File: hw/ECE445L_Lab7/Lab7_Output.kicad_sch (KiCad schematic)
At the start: 4 parts, among them Q1 IRLD024PBF, U2 Adafruit ST7735R

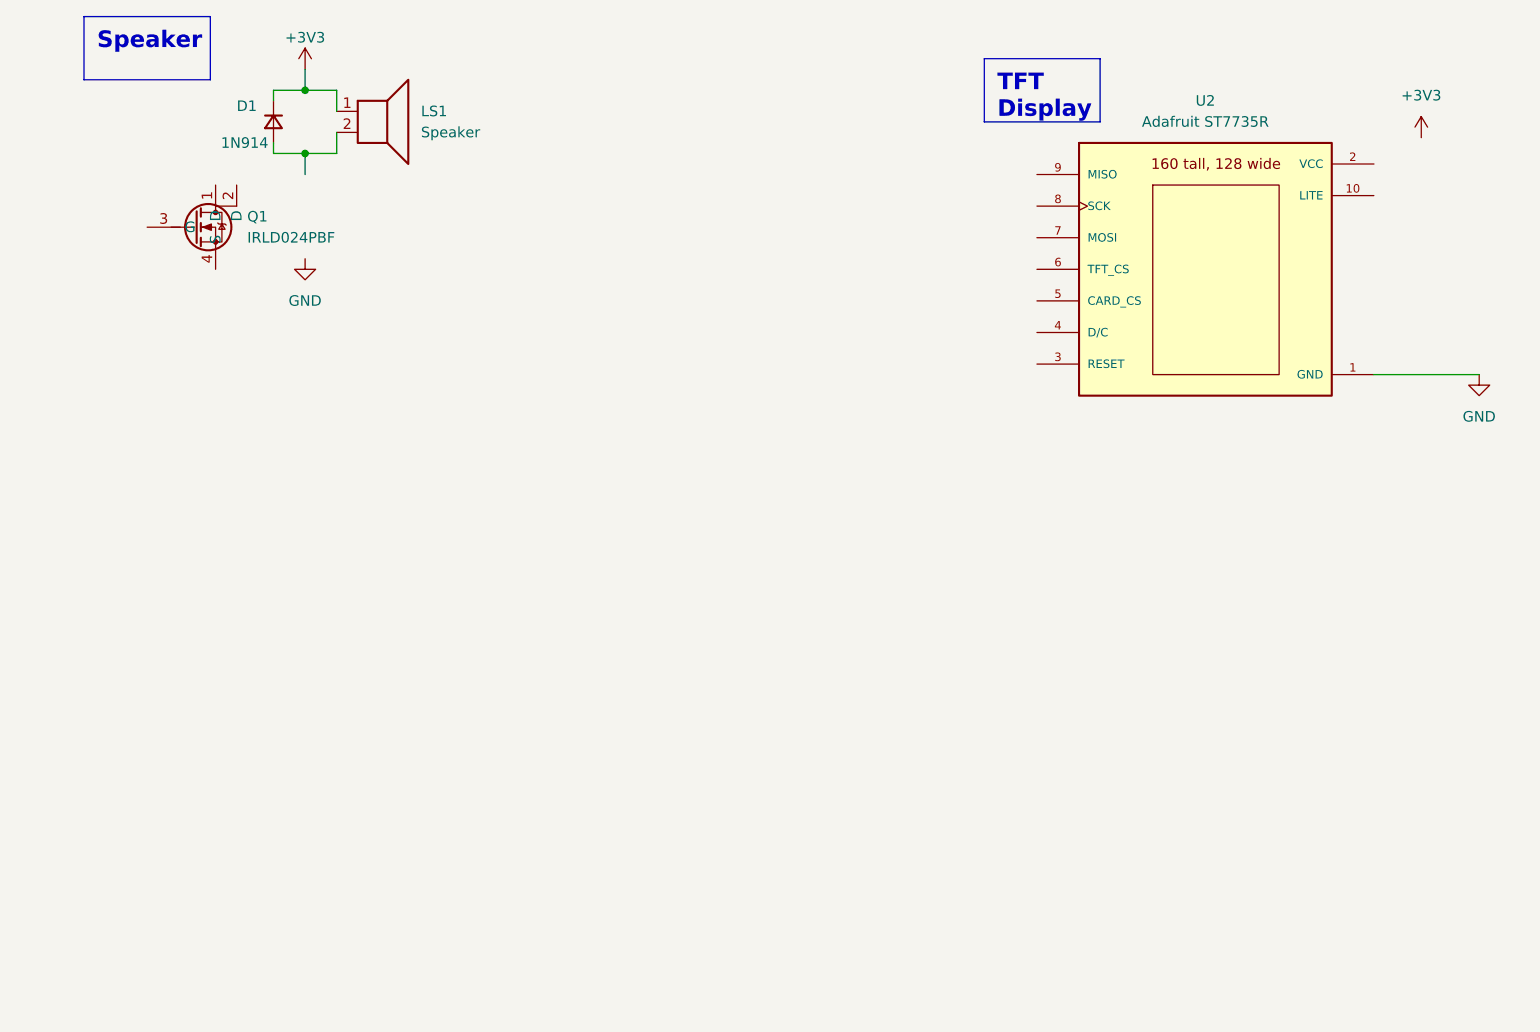
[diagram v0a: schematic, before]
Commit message: Created spice models for analog circuits, started kicad schematic -> right audio channel, screen, basic power
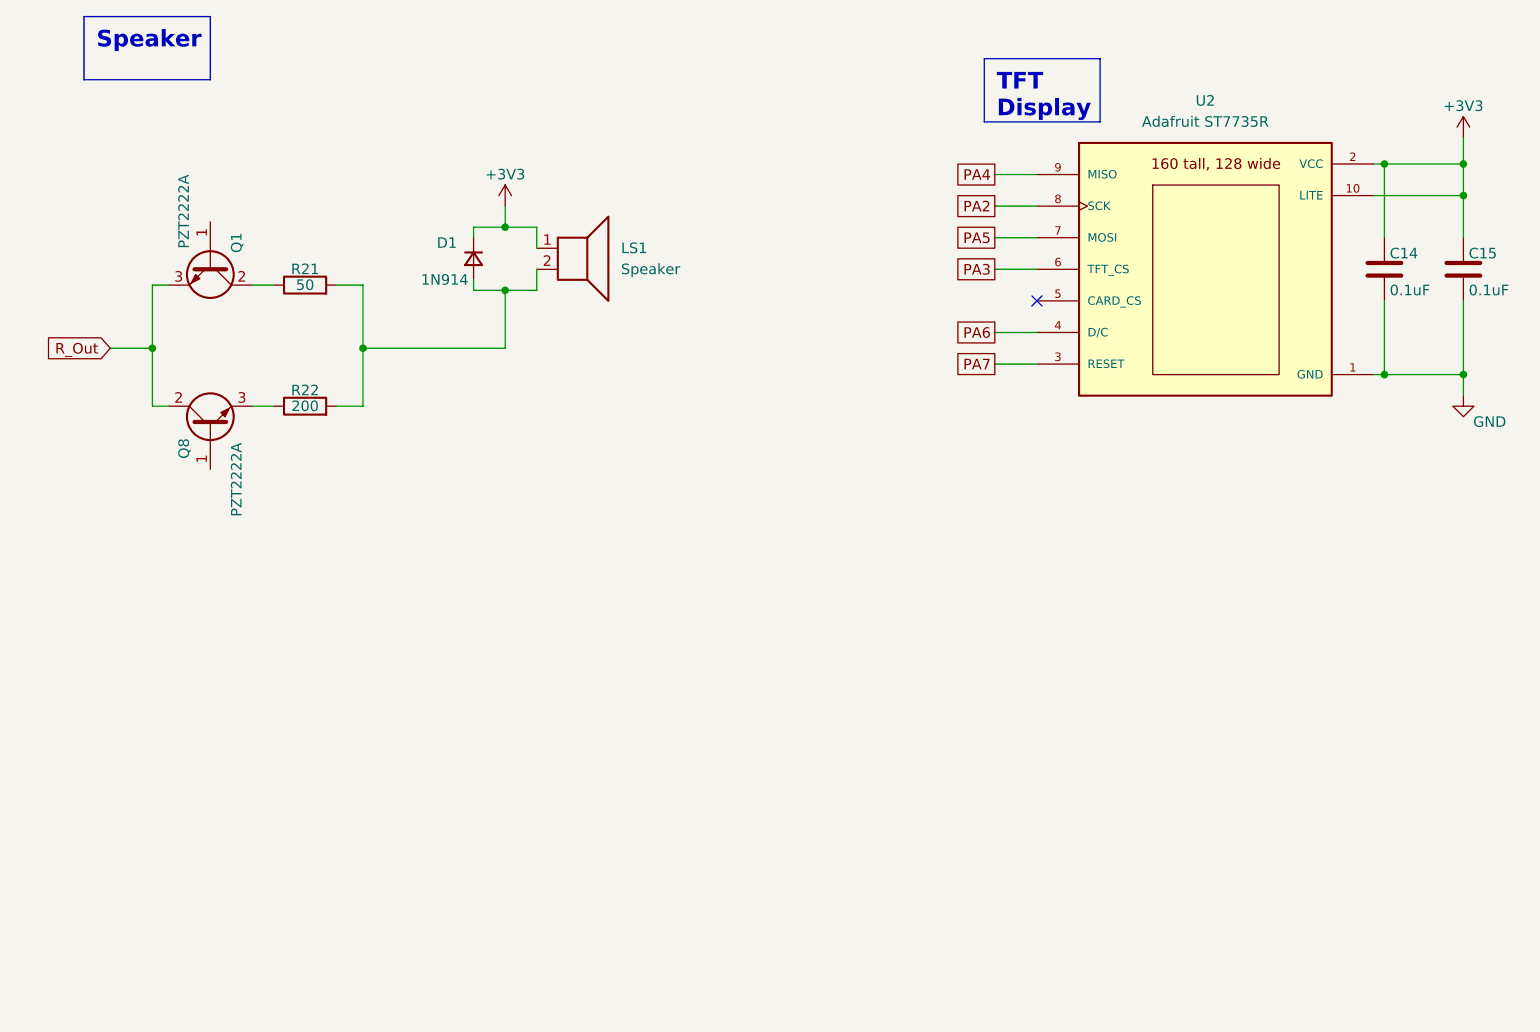
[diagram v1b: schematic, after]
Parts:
- removed Q1: IRLD024PBF, ECE445L:DIP920W60P254L490H457Q4N, symbol ECE445L:IRLD024PBF
- added C14, C15: 0.1uF, ECE445L:C_Axial_200mil, symbol ECE445L:C
- added Q1, Q8: PZT2222A, Package_TO_SOT_SMD:SOT-223-3_TabPin2, symbol Transistor_BJT:PZT2222A
- added R21: 50, Resistor_SMD:R_0805_2012Metric, symbol Device:R
- added R22: 200, Resistor_SMD:R_0805_2012Metric, symbol Device:R
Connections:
- net +3V3: now also U2.10 (LITE), U2.2 (VCC), C14.1, C15.1
- net GND: now also C14.2, C15.2
- net at D1.2 (A), LS1.2: now also R21.2, R22.2
- net PA7: now reaches U2.3 (RESET)
- net PA6: now reaches U2.4 (D/C)
- net PA3: now reaches U2.6 (TFT_CS)
- net PA5: now reaches U2.7 (MOSI)
- net PA2: now reaches U2.8 (SCK)
- net PA4: now reaches U2.9 (MISO)
- new net: Q8.3 (E), R22.1
- new net: Q1.2 (C), R21.1
- new net R_Out: Q1.3 (E), Q8.2 (C)
- no-connect marks 0 -> 1
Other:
- moved on the sheet: D1, LS1

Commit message: Updated hardware schematic
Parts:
- removed D1: 1N914, ECE445L:D_P6.35mm_Horizontal, symbol ECE445L:D_Small
- removed LS1: Speaker, ECE445L:PinHeader_1x02_P2.54mm_Vertical, symbol ECE445L:Speaker
- added J2: AudioJack, ECE445L:Jack_3.5mm_CUI_SJ1-3523N_Horizontal, symbol ECE445L:HeadphoneJack
- added Q15, Q16: PZT2222A, Package_TO_SOT_SMD:SOT-223-3_TabPin2, symbol Transistor_BJT:PZT2222A
- added R42: 50, Resistor_SMD:R_0805_2012Metric, symbol Device:R
- added R43: 200, Resistor_SMD:R_0805_2012Metric, symbol Device:R
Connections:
- net GND: now also J2.S (sleeve)
- net at R21.2, R22.2: now also J2.T (tip)
- net PF1: now reaches Q8.1 (B)
- net PF1: now also Q16.1 (B)
- net PF0: now reaches Q1.1 (B)
- net PF0: now also Q15.1 (B)
- new net: Q15.2 (C), R42.1
- new net: J2.R (ring), R42.2, R43.2
- new net: Q16.3 (E), R43.1
- new net L_Out: Q15.3 (E), Q16.2 (C)

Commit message: Lab7A Schematic and BOM - Ashton
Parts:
- removed Q1, Q15, Q16, Q8: PZT2222A, Package_TO_SOT_SMD:SOT-223-3_TabPin2, symbol Transistor_BJT:PZT2222A
- removed R21, R42: 50, Resistor_SMD:R_0805_2012Metric, symbol Device:R
- removed R22, R43: 200, Resistor_SMD:R_0805_2012Metric, symbol Device:R
- added D1, D2: 1N914, symbol Device:D
- added D3, D4: LED, ECE445L:LED_D5.0mm, symbol ECE445L:LED
- added R58, R59: 50, Resistor_SMD:R_0805_2012Metric, symbol Device:R
- added R78, R79: 2k, Resistor_SMD:R_0805_2012Metric, symbol Device:R
- renumbered C14 to C38, C15 to C39, U2 to U16
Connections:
- net GND: now also D1.2 (A), D2.2 (A), D3.1 (K), D4.1 (K)
- net at J2.R (ring): now also D2.1 (K), R59.1
- net at J2.T (tip): now also D1.1 (K), R58.1
- new net: D3.2 (A), R78.2
- new net: D4.2 (A), R79.2
- new net L_AudioOut: R59.2
- new net PB3: R78.1, R79.1
- new net R_AudioOut: R58.2
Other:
- moved on the sheet: J2

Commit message: Made changers to the schematic, updated bom, and created priliminary layout for the PCB. Ready for 7B Prep!
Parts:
- C38, C39: footprint ECE445L:C_Axial_200mil -> Capacitor_SMD:C_0603_1608Metric
- R58, R59, R78, R79: footprint Resistor_SMD:R_0805_2012Metric -> Resistor_SMD:R_0603_1608Metric
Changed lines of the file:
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@@
 			)
 		)
-		(property "Footprint" "ECE445L:C_Axial_200mil"
+		(property "Footprint" "Capacitor_SMD:C_0603_1608Metric"
 			(at 190.8302 55.245 0)
 			(effects
@@
 			)
 		)
-		(property "Footprint" "ECE445L:C_Axial_200mil"
+		(property "Footprint" "Capacitor_SMD:C_0603_1608Metric"
 			(at 181.3052 55.245 0)
 			(effects
@@
 			)
 		)
-		(property "Footprint" "Resistor_SMD:R_0805_2012Metric"
+		(property "Footprint" "Resistor_SMD:R_0603_1608Metric"
 			(at 29.972 80.645 90)
 			(effects
@@
 			)
 		)
-		(property "Footprint" "Resistor_SMD:R_0805_2012Metric"
+		(property "Footprint" "Resistor_SMD:R_0603_1608Metric"
 			(at 42.672 80.645 90)
 			(effects
@@
 			)
 		)
-		(property "Footprint" "Resistor_SMD:R_0805_2012Metric"
+		(property "Footprint" "Resistor_SMD:R_0603_1608Metric"
 			(at 39.37 31.877 90)
 			(effects
@@
 			)
 		)
-		(property "Footprint" "Resistor_SMD:R_0805_2012Metric"
+		(property "Footprint" "Resistor_SMD:R_0603_1608Metric"
 			(at 38.735 52.832 90)
 			(effects

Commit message: Rough draft layout - need to remove tm4c chip
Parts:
- C39: renamed from C38; footprint Capacitor_SMD:C_0603_1608Metric -> Capacitor_SMD:C_0603_1608Metric_Pad1.08x0.95mm_HandSolder
- C40: renamed from C39; footprint Capacitor_SMD:C_0603_1608Metric -> Capacitor_SMD:C_0603_1608Metric_Pad1.08x0.95mm_HandSolder
- D3: renamed from D1; footprint (none) -> ECE445L:Testpoint_1x02_P2.54mm
- D4: renamed from D2; footprint (none) -> ECE445L:Testpoint_1x02_P2.54mm
- R85: renamed from R78; footprint Resistor_SMD:R_0603_1608Metric -> Resistor_SMD:R_0603_1608Metric_Pad0.98x0.95mm_HandSolder
- R86: renamed from R59; footprint Resistor_SMD:R_0603_1608Metric -> Resistor_SMD:R_0603_1608Metric_Pad0.98x0.95mm_HandSolder
- R87: renamed from R58; footprint Resistor_SMD:R_0603_1608Metric -> Resistor_SMD:R_0603_1608Metric_Pad0.98x0.95mm_HandSolder
- R88: renamed from R79; footprint Resistor_SMD:R_0603_1608Metric -> Resistor_SMD:R_0603_1608Metric_Pad0.98x0.95mm_HandSolder
- renumbered D3 to D1, D4 to D2, J2 to J4
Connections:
- net PB3 renamed PD6
- net PD6: no longer R88.1
- new net PD7: R88.1
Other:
- company: (none) -> The University of Texas at Austin
- title: (none) -> ECE 445L Lab7
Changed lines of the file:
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@@
 	(generator_version "9.0")
 	(paper "A4")
+	(title_block
+		(title "ECE 445L Lab7")
+		(date "2025-10-31")
+		(rev "v1.0.0")
+		(company "The University of Texas at Austin")
+		(comment 1 "Drawn By Ashton Knecht - atk836")
+	)
 	(text_box "TFT Display"
 		(exclude_from_sim no)
@@
 		)
 	)
-	(global_label "PB3"
+	(global_label "PD7"
 		(shape passive)
 		(at 44.45 73.025 90)
@@
 		)
 	)
-	(global_label "PB3"
+	(global_label "PD6"
 		(shape passive)
 		(at 31.75 73.025 90)
@@
 		(dnp no)
 		(fields_autoplaced yes)
-		(property "Reference" "D3"
+		(property "Reference" "D1"
 			(at 35.56 93.0274 0)
 			(effects
@@
 			(project ""
 				(path "/69b823fd-c065-40ff-9bb9-c5835555f3eb/a500a078-11dc-409b-bff9-a8c35e1dabf8"
-					(reference "D3")
+					(reference "D1")
 					(unit 1)
 				)
@@
 		(on_board yes)
 		(dnp no)
-		(property "Reference" "#PWR035"
+		(property "Reference" "#PWR0106"
 			(at 189.865 73.025 0)
 			(effects
@@
 			(project "ECE445L_Lab7"
 				(path "/69b823fd-c065-40ff-9bb9-c5835555f3eb/a500a078-11dc-409b-bff9-a8c35e1dabf8"
-					(reference "#PWR035")
+					(reference "#PWR0106")
 					(unit 1)
 				)
@@
 		(dnp no)
 		(fields_autoplaced yes)
-		(property "Reference" "D1"
+		(property "Reference" "D3"
 			(at 50.165 37.4649 90)
 			(effects
@@
 			)
 		)
-		(property "Footprint" ""
+		(property "Footprint" "ECE445L:Testpoint_1x02_P2.54mm"
 			(at 47.625 38.735 0)
 			(effects
@@
 			(project ""
 				(path "/69b823fd-c065-40ff-9bb9-c5835555f3eb/a500a078-11dc-409b-bff9-a8c35e1dabf8"
-					(reference "D1")
+					(reference "D3")
 					(unit 1)
 				)
@@
 		(on_board yes)
 		(dnp no)
-		(property "Reference" "#PWR034"
+		(property "Reference" "#PWR0105"
 			(at 189.865 39.37 0)
 			(effects
@@
 			(project "ECE445L_Lab7"
 				(path "/69b823fd-c065-40ff-9bb9-c5835555f3eb/a500a078-11dc-409b-bff9-a8c35e1dabf8"
-					(reference "#PWR034")
+					(reference "#PWR0105")
 					(unit 1)
 				)
@@
 		(on_board yes)
 		(dnp no)
-		(property "Reference" "C39"
+		(property "Reference" "C40"
 			(at 190.5 49.53 0)
 			(effects
@@
 			)
 		)
-		(property "Footprint" "Capacitor_SMD:C_0603_1608Metric"
+		(property "Footprint" "Capacitor_SMD:C_0603_1608Metric_Pad1.08x0.95mm_HandSolder"
 			(at 190.8302 55.245 0)
 			(effects
@@
 			(project "ECE445L_Lab7"
 				(path "/69b823fd-c065-40ff-9bb9-c5835555f3eb/a500a078-11dc-409b-bff9-a8c35e1dabf8"
-					(reference "C39")
+					(reference "C40")
 					(unit 1)
 				)
@@
 		(dnp no)
 		(fields_autoplaced yes)
-		(property "Reference" "D4"
+		(property "Reference" "D2"
 			(at 48.26 93.0274 0)
 			(effects
@@
 			(project "ECE445L_Lab7"
 				(path "/69b823fd-c065-40ff-9bb9-c5835555f3eb/a500a078-11dc-409b-bff9-a8c35e1dabf8"
-					(reference "D4")
+					(reference "D2")
 					(unit 1)
 				)
@@
 		(on_board yes)
 		(dnp no)
-		(property "Reference" "#PWR06"
+		(property "Reference" "#PWR0104"
 			(at 38.735 109.855 0)
 			(effects
@@
 			(project "ECE445L_Lab7"
 				(path "/69b823fd-c065-40ff-9bb9-c5835555f3eb/a500a078-11dc-409b-bff9-a8c35e1dabf8"
-					(reference "#PWR06")
+					(reference "#PWR0104")
 					(unit 1)
 				)
@@
 		(on_board yes)
 		(dnp no)
-		(property "Reference" "C38"
+		(property "Reference" "C39"
 			(at 180.975 49.53 0)
 			(effects
@@
 			)
 		)
-		(property "Footprint" "Capacitor_SMD:C_0603_1608Metric"
+		(property "Footprint" "Capacitor_SMD:C_0603_1608Metric_Pad1.08x0.95mm_HandSolder"
 			(at 181.3052 55.245 0)
 			(effects
@@
 			(project "ECE445L_Lab7"
 				(path "/69b823fd-c065-40ff-9bb9-c5835555f3eb/a500a078-11dc-409b-bff9-a8c35e1dabf8"
-					(reference "C38")
+					(reference "C39")
 					(unit 1)
 				)
@@
 		(dnp no)
 		(fields_autoplaced yes)
-		(property "Reference" "J2"
+		(property "Reference" "J4"
 			(at 72.39 42.5449 0)
 			(effects
@@
 			(project ""
 				(path "/69b823fd-c065-40ff-9bb9-c5835555f3eb/a500a078-11dc-409b-bff9-a8c35e1dabf8"
-					(reference "J2")
+					(reference "J4")
 					(unit 1)
 				)
@@
 		(on_board yes)
 		(dnp no)
-		(property "Reference" "R78"
+		(property "Reference" "R85"
 			(at 34.29 78.74 90)
 			(effects
@@
 			)
 		)
-		(property "Footprint" "Resistor_SMD:R_0603_1608Metric"
+		(property "Footprint" "Resistor_SMD:R_0603_1608Metric_Pad0.98x0.95mm_HandSolder"
 			(at 29.972 80.645 90)
 			(effects
@@
 			(project "ECE445L_Lab7"
 				(path "/69b823fd-c065-40ff-9bb9-c5835555f3eb/a500a078-11dc-409b-bff9-a8c35e1dabf8"
-					(reference "R78")
+					(reference "R85")
 					(unit 1)
 				)
@@
 		(dnp no)
 		(fields_autoplaced yes)
-		(property "Reference" "D2"
+		(property "Reference" "D4"
 			(at 50.165 48.2599 90)
 			(effects
@@
 			)
 		)
-		(property "Footprint" ""
+		(property "Footprint" "ECE445L:Testpoint_1x02_P2.54mm"
 			(at 47.625 49.53 0)
 			(effects
@@
 			(project "ECE445L_Lab7"
 				(path "/69b823fd-c065-40ff-9bb9-c5835555f3eb/a500a078-11dc-409b-bff9-a8c35e1dabf8"
-					(reference "D2")
+					(reference "D4")
 					(unit 1)
 				)
@@
 		(on_board yes)
 		(dnp no)
-		(property "Reference" "R79"
+		(property "Reference" "R88"
 			(at 46.99 78.74 90)
 			(effects
@@
 			)
 		)
-		(property "Footprint" "Resistor_SMD:R_0603_1608Metric"
+		(property "Footprint" "Resistor_SMD:R_0603_1608Metric_Pad0.98x0.95mm_HandSolder"
 			(at 42.672 80.645 90)
 			(effects
@@
 			(project "ECE445L_Lab7"
 				(path "/69b823fd-c065-40ff-9bb9-c5835555f3eb/a500a078-11dc-409b-bff9-a8c35e1dabf8"
-					(reference "R79")
+					(reference "R88")
 					(unit 1)
 				)
@@
 		(on_board yes)
 		(dnp no)
-		(property "Reference" "R58"
+		(property "Reference" "R87"
 			(at 41.275 36.195 90)
 			(effects
@@
 			)
 		)
-		(property "Footprint" "Resistor_SMD:R_0603_1608Metric"
+		(property "Footprint" "Resistor_SMD:R_0603_1608Metric_Pad0.98x0.95mm_HandSolder"
 			(at 39.37 31.877 90)
 			(effects
@@
 			(project "ECE445L_Lab7"
 				(path "/69b823fd-c065-40ff-9bb9-c5835555f3eb/a500a078-11dc-409b-bff9-a8c35e1dabf8"
-					(reference "R58")
+					(reference "R87")
 					(unit 1)
 				)
@@
 		(on_board yes)
 		(dnp no)
-		(property "Reference" "#PWR01"
+		(property "Reference" "#PWR0103"
 			(at 38.735 50.8 0)
 			(effects
@@
 			(project ""
 				(path "/69b823fd-c065-40ff-9bb9-c5835555f3eb/a500a078-11dc-409b-bff9-a8c35e1dabf8"
-					(reference "#PWR01")
+					(reference "#PWR0103")
 					(unit 1)
 				)
@@
 		(on_board yes)
 		(dnp no)
-		(property "Reference" "R59"
+		(property "Reference" "R86"
 			(at 40.64 57.15 90)
 			(effects
@@
 			)
 		)
-		(property "Footprint" "Resistor_SMD:R_0603_1608Metric"
+		(property "Footprint" "Resistor_SMD:R_0603_1608Metric_Pad0.98x0.95mm_HandSolder"
 			(at 38.735 52.832 90)
 			(effects
@@
 			(project "ECE445L_Lab7"
 				(path "/69b823fd-c065-40ff-9bb9-c5835555f3eb/a500a078-11dc-409b-bff9-a8c35e1dabf8"
-					(reference "R59")
+					(reference "R86")
 					(unit 1)
 				)

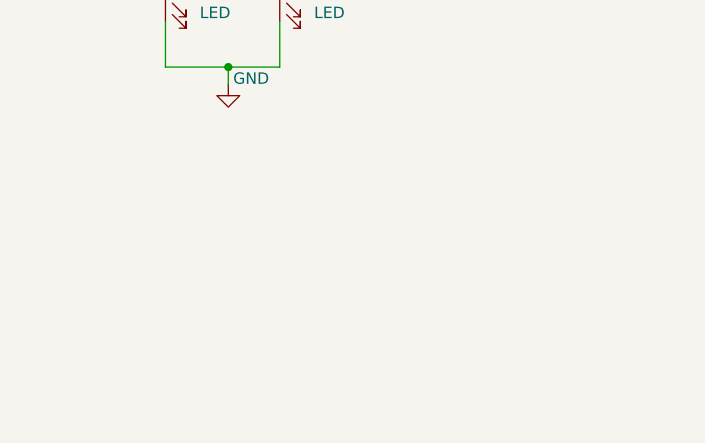
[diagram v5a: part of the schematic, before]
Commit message: Added current consumption to schematic
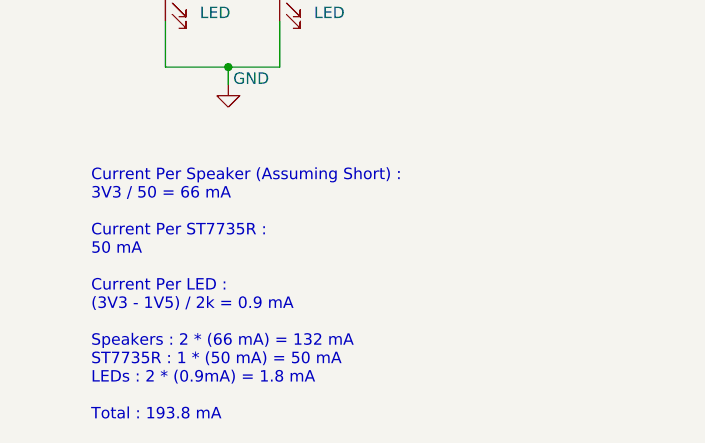
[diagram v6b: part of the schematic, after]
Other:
- note added: "Current Per Speaker (Assuming Short) : 3V3 / 50 = 66 mA Current Per ST7735R : 50 mA Current Per LED : (3V3 - 1V5) / 2k = 0.9 mA Speakers : 2 * (66 mA) = 132 mA ST7735R : 1 * (50 mA) = 50 mA LEDs : 2 * (0.9mA) = 1.8 mA Total : 193.8 mA"
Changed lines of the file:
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@@
 		(comment 1 "Drawn By Ashton Knecht - atk836")
+	)
+	(text "Current Per Speaker (Assuming Short) :\n3V3 / 50 = 66 mA\n\nCurrent Per ST7735R :\n50 mA\n\nCurrent Per LED :\n(3V3 - 1V5) / 2k = 0.9 mA\n\nSpeakers : 2 * (66 mA) = 132 mA\nST7735R : 1 * (50 mA) = 50 mA\nLEDs : 2 * (0.9mA) = 1.8 mA\n\nTotal : 193.8 mA\n"
+		(exclude_from_sim no)
+		(at 23.495 127 0)
+		(effects
+			(font
+				(size 1.27 1.27)
+			)
+			(justify left)
+		)
 	)
 	(text_box "TFT Display"

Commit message: PCB Layout
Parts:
- R85: value 2k -> 1.5k
- R88: value 2k -> 1.5V
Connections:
- net +3V3: now also R85.1, R88.1
- net GND: no longer D1.1 (K), D2.1 (K)
- net PD6: now also D1.1 (K); no longer R85.1
- net PD7: now also D2.1 (K); no longer R88.1
